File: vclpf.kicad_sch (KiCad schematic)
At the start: 48 parts, among them J1 NJ2FD-V, J2 NJ2FD-V, J3 NJ2FD-V, Q1 2N3904, Q2 2N3906, Q3 2N3904, Q4 2N3906, U1 ADA4084-4xCP, U2 ADA4084-4xCP

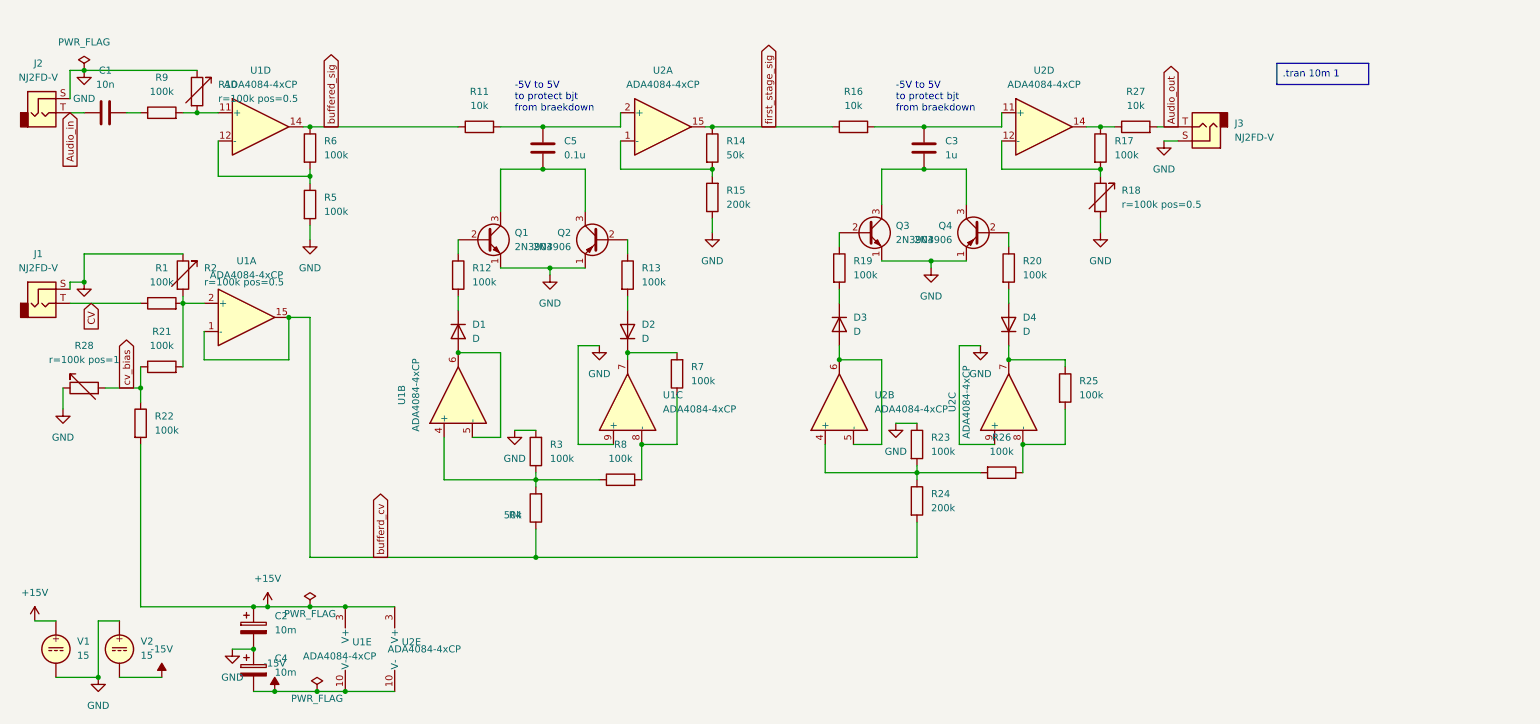
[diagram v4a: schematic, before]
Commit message: add resonance
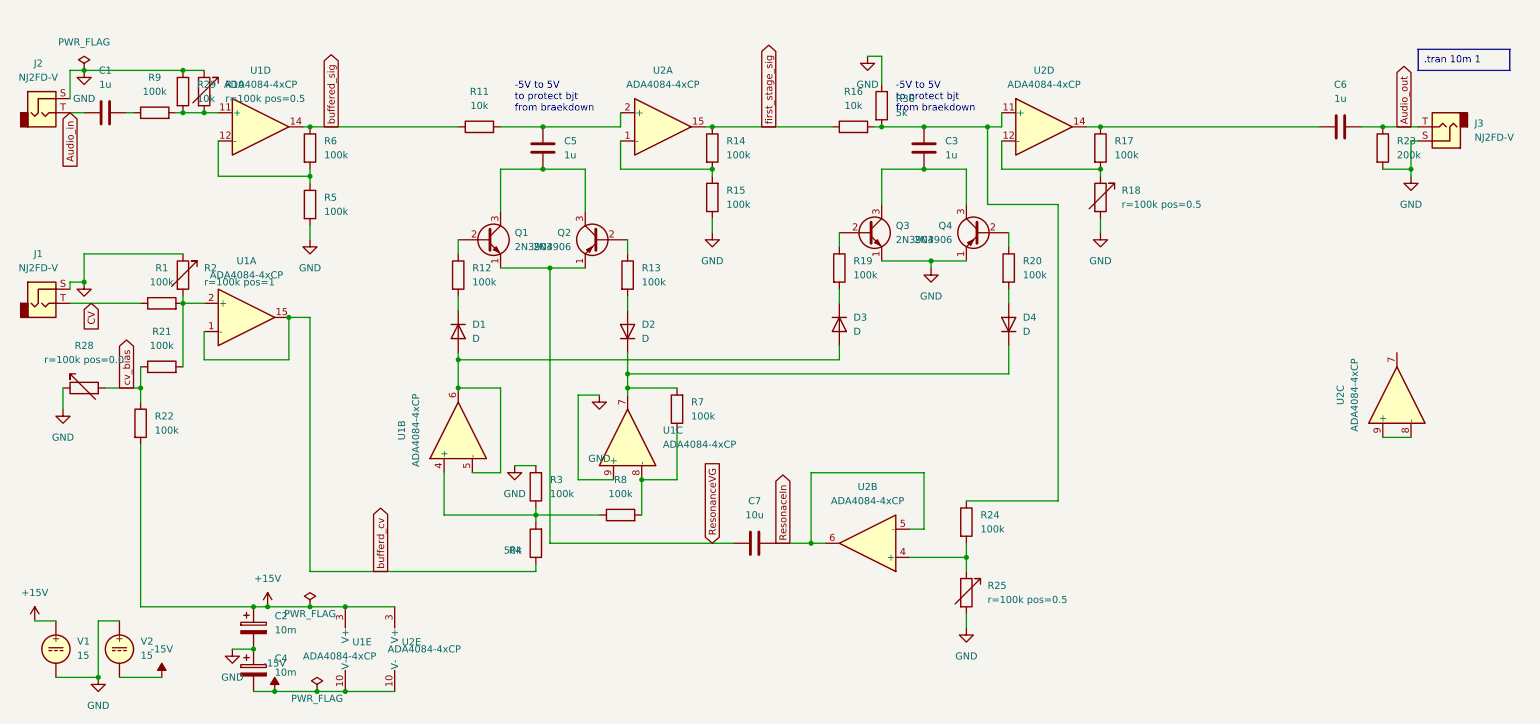
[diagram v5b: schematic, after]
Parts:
- removed R25, R26: 100k, symbol Device:R
- removed R27: 10k, symbol Device:R
- added C6: 1u, symbol Device:C
- added C7: 10u, symbol Device:C
- added R25: ${SIM.PARAMS}, symbol Device:R_Variable
- added R29: 10k, symbol Device:R
- added R30: 5k, symbol Device:R
- C1: value 10n -> 1u
- C5: value 0.1u -> 1u
- R14: value 50k -> 100k
- R15, R24: value 200k -> 100k
- R23: value 100k -> 200k
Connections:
- net Audio_out: now also R23.1, C6.2
- net GND: now also R23.2, R25.2, R29.1, R30.1; no longer Q1.1 (E), Q2.1 (E), R23.1, U2.9 (+)
- net bufferd_cv: no longer R24.2
- net at R10.2, R9.2, U1.11 (+): now also R29.2
- net at D1.2 (A), U1.5 (-), U1.6: now also D3.2 (A)
- net ResonaceIn: now reaches U2.5 (-), U2.6
- net ResonaceIn: now also C7.2; no longer D3.2 (A)
- net at D2.1 (K), R7.2, U1.7: now also D4.1 (K)
- net at U2.7: no longer D4.1 (K)
- net at U2.8 (-): now also U2.9 (+)
- net at C3.1, R16.2, U2.11 (+): now also R24.1, R30.2
- net at R17.1, U2.14: now also C6.1
- new net: R24.2, R25.1, U2.4 (+)
- new net ResonanceVG: C7.1, Q1.1 (E), Q2.1 (E)
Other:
- moved on the sheet: J3, R10, R3, R4, R7, R8, R9, U1B, U1C, U2B, U2C
